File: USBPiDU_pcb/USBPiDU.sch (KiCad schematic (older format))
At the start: 29 parts

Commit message: Redid load ports with AP22802 load switch
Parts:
- removed D? (x5): LED, symbol LED
- removed J? (x5): USB_A, symbol USB_A
- removed R? (x5): 1k, symbol R
- added D? (x5): LED, symbol LED
- added J? (x5): USB_A, symbol USB_A
- added J?: Load Rail Input, symbol Screw_Terminal_1x02
- added R? (x5): 1k, symbol R
- added U? (x5): AP22802, symbol AP22802
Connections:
- net GND: now also J?.2, J?.4 (GND), J?.4 (GND), J?.4 (GND), J?.4 (GND), J?.4 (GND), J?.5 (Shield), J?.5 (Shield), J?.5 (Shield), J?.5 (Shield), J?.5 (Shield), R?.2, R?.2, R?.2, R?.2, R?.2, U?.2 (GND), U?.2 (GND), U?.2 (GND), U?.2 (GND), U?.2 (GND)
- net P1_CTL: now also U?.4 (EN)
- net P2_CTL: now also U?.4 (EN)
- net P3_CTL: now also U?.4 (EN)
- net P4_CTL: now also U?.4 (EN)
- net P5_CTL: now also U?.4 (EN)
- net +5VP: now reaches D?.2 (A), J?.1 (VBUS)
- net +5VP: now also J?.1, U?.5 (IN), U?.5 (IN), U?.5 (IN), U?.5 (IN), U?.5 (IN)
- new net: D?.2 (A), J?.1 (VBUS), U?.1 (OUT) (x5)
- new net: J?.2 (D-), J?.3 (D+) (x5)
- new net: D?.1 (K), R?.1 (x5)
- new net FAULT: U?.3 (FLG), U?.3 (FLG), U?.3 (FLG), U?.3 (FLG), U?.3 (FLG)

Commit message: First wag at board layout
Will probably end up changing port control pinout to improve routing
and add random IO headers to eat up the rest of the GPIO and board space
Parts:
- added MK1, MK2, MK3, MK4: Mounting_Hole_PAD, Mounting_Holes:MountingHole_2.7mm_M2.5_Pad_Via, symbol Mounting_Hole_PAD
- C1, C2, C3, C4: renamed from C?; footprint (none) -> Capacitors_SMD:C_0603_HandSoldering
- D1, D2, D3, D4, D5, D6: renamed from D?; footprint (none) -> LEDs:LED_0603
- J1: renamed from J?; value USB_OTG -> 609-4613-1-ND; footprint (none) -> USP-PiDU:USB_MicroB_SMT
- J2: renamed from J?; footprint (none) -> Pin_Headers:Pin_Header_Straight_2x03_Pitch2.54mm
- J3: renamed from J?; footprint (none) -> Connectors_Phoenix:PhoenixContact_MSTBVA-G_02x5.00mm_Vertical
- L1: renamed from L?; footprint (none) -> Inductors_SMD:L_1206_Handsoldering
- P1, P2, P3, P4, P5, P6: renamed from J?; footprint (none) -> USP-PiDU:USB_A_RightAngle_side
- R1, R3, R4, R5, R6, R7, R8: renamed from R?; footprint (none) -> Resistors_SMD:R_0603_HandSoldering
- U1: renamed from U?; footprint SSOP-28 -> Housings_SSOP:SSOP-28_5.3x10.2mm_Pitch0.65mm
- U2: renamed from U?; footprint TQFP32 -> Housings_QFP:TQFP-32_7x7mm_Pitch0.8mm
- U3, U4, U5, U6, U7: renamed from U?; footprint (none) -> USP-PiDU:SOT-25-5
- Y1: renamed from Y?; footprint (none) -> Crystals:Crystal_SMD_HC49-SD
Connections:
- net GND: now also MK1.1, MK2.1, MK3.1, MK4.1
- removed net FAULT: U3.3 (FLG), U4.3 (FLG), U5.3 (FLG), U6.3 (FLG), U7.3 (FLG)
- no-connect marks 14 -> 20
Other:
- moved on the sheet: D1, D2, D3, D4, D5, D6, P1, P2, P3, P4, P5, P6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

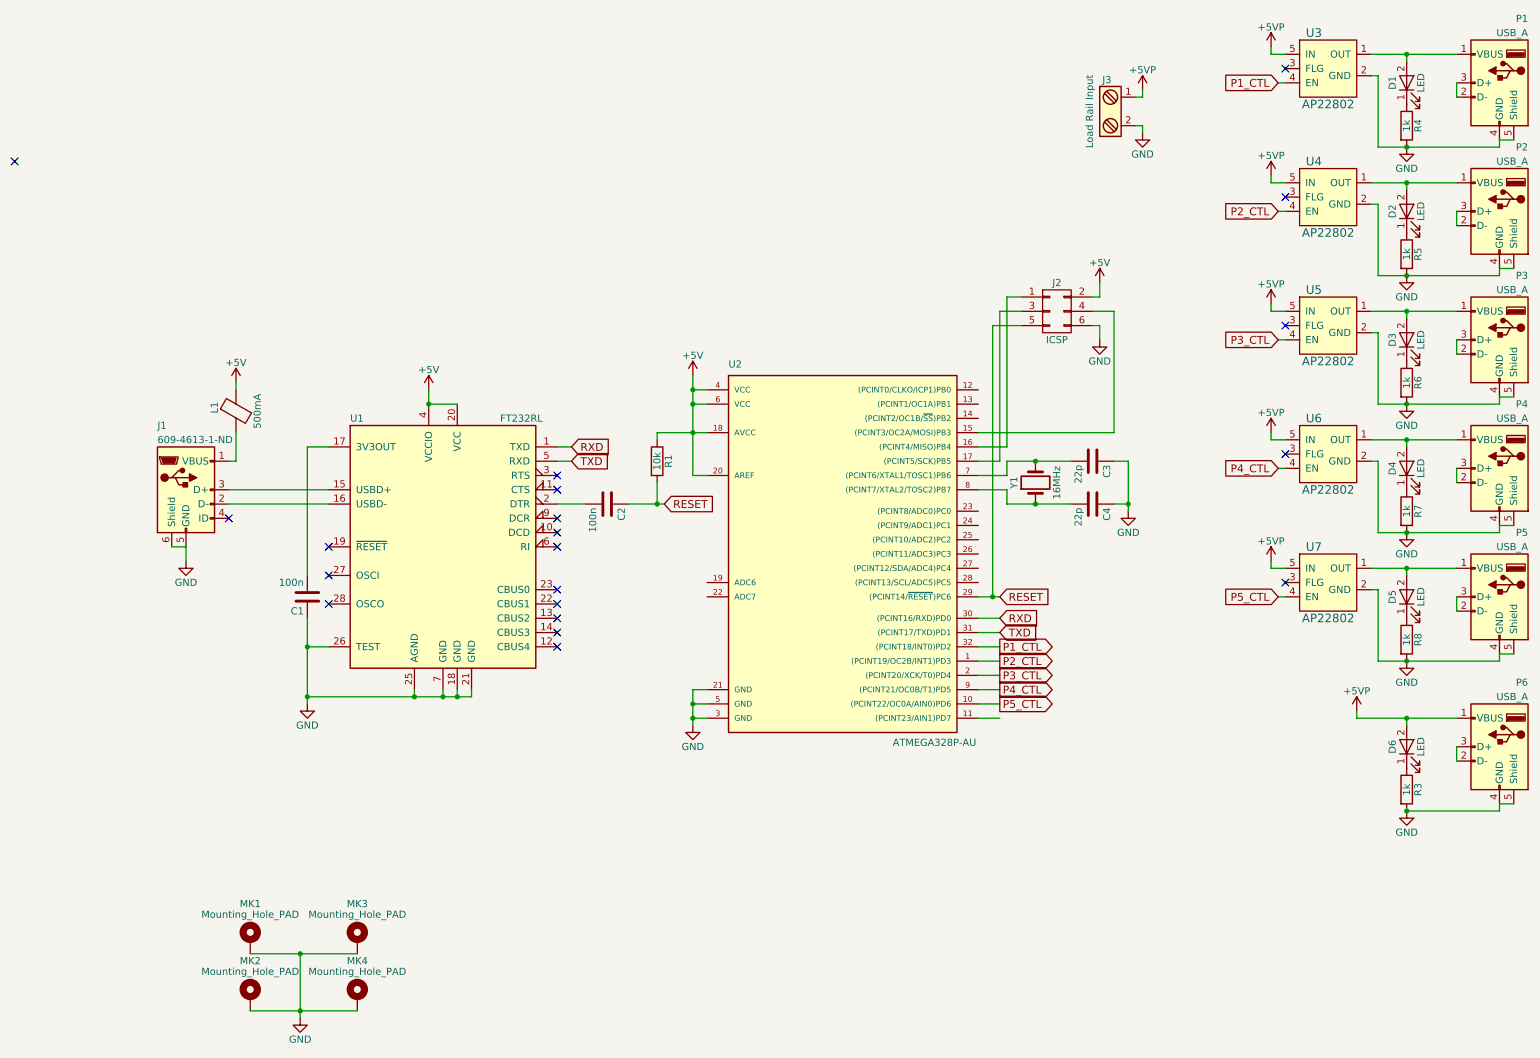
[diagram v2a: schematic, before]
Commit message: Final v0.1 board layout
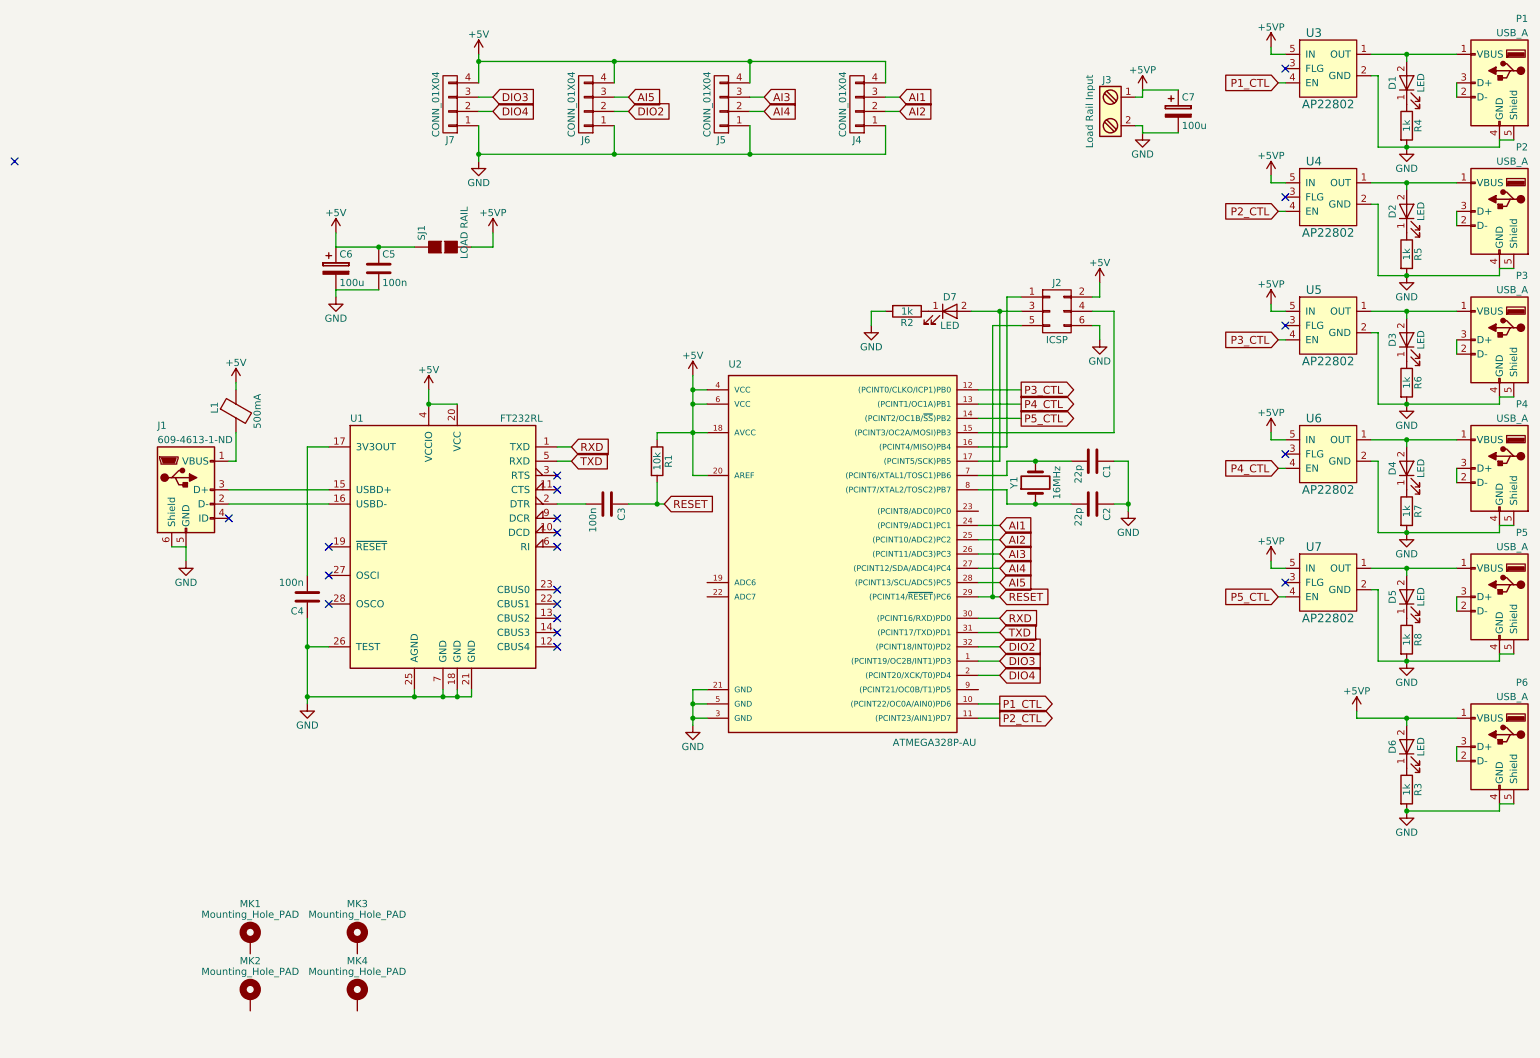
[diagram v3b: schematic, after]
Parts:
- added C5: 100n, Capacitors_SMD:C_0603_HandSoldering, symbol C
- added C6, C7: 100u, Capacitors_Tantalum_SMD:CP_Tantalum_Case-X_EIA-7343-43_Hand, symbol CP
- added D7: LED, LEDs:LED_0603, symbol LED
- added J4, J5, J6, J7: CONN_01X04, Pin_Headers:Pin_Header_Straight_1x04_Pitch2.54mm, symbol CONN_01X04
- added R2: 1k, Resistors_SMD:R_0603_HandSoldering, symbol R
- added SJ1: LOAD RAIL, Connectors:GS2, symbol GS2
- renumbered C3 to C1, C4 to C2, C2 to C3, C1 to C4
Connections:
- net +5V: now also C5.1, C6.1, J4.4 (P4), J5.4 (P4), J6.4 (P4), J7.4 (P4), SJ1.1 (G1)
- net +5VP: now also C7.1, SJ1.2 (G2)
- net GND: now also C5.2, C6.2, C7.2, J4.1 (P1), J5.1 (P1), J6.1 (P1), J7.1 (P1), R2.2; no longer MK1.1, MK2.1, MK3.1, MK4.1
- net P1_CTL: now also U2.10 ((PCINT22/OC0A/AIN0)PD6); no longer U2.32 ((PCINT18/INT0)PD2)
- net P2_CTL: now also U2.11 ((PCINT23/AIN1)PD7); no longer U2.1 ((PCINT19/OC2B/INT1)PD3)
- net P3_CTL: now also U2.12 ((PCINT0/CLKO/ICP1)PB0); no longer U2.2 ((PCINT20/XCK/T0)PD4)
- net P4_CTL: now also U2.13 ((PCINT1/OC1A)PB1); no longer U2.9 ((PCINT21/OC0B/T1)PD5)
- net P5_CTL: now also U2.14 ((PCINT2/OC1B/~SS~)PB2); no longer U2.10 ((PCINT22/OC0A/AIN0)PD6)
- net at J2.3 (P3), U2.17 ((PCINT5/SCK)PB5): now also D7.2 (A)
- net AI1: now reaches U2.24 ((PCINT9/ADC1)PC1)
- net AI1: now also J4.3 (P3)
- net AI2: now reaches U2.25 ((PCINT10/ADC2)PC2)
- net AI2: now also J4.2 (P2)
- net AI3: now reaches U2.26 ((PCINT11/ADC3)PC3)
- net AI3: now also J5.3 (P3)
- net AI4: now reaches U2.27 ((PCINT12/SDA/ADC4)PC4)
- net AI4: now also J5.2 (P2)
- net AI5: now reaches U2.28 ((PCINT13/SCL/ADC5)PC5)
- net AI5: now also J6.3 (P3)
- new net: D7.1 (K), R2.1
- new net DIO2: J6.2 (P2), U2.32 ((PCINT18/INT0)PD2)
- new net DIO3: J7.3 (P3), U2.1 ((PCINT19/OC2B/INT1)PD3)
- new net DIO4: J7.2 (P2), U2.2 ((PCINT20/XCK/T0)PD4)
